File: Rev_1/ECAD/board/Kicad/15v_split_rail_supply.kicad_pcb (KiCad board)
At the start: 4 copper layers, 71.1 x 36.8 mm, 89 parts, among them Q1 NPN, Q100 IPP029N15NM6, Q101 NPN, Q102 NPN, Q103 PMOS, Q2 NPN, U100 LM3478MA, U2 LM358, U3 LM358, U4 SN74AHC1G02DBVR, U5 SN74AHC1G02DBVR

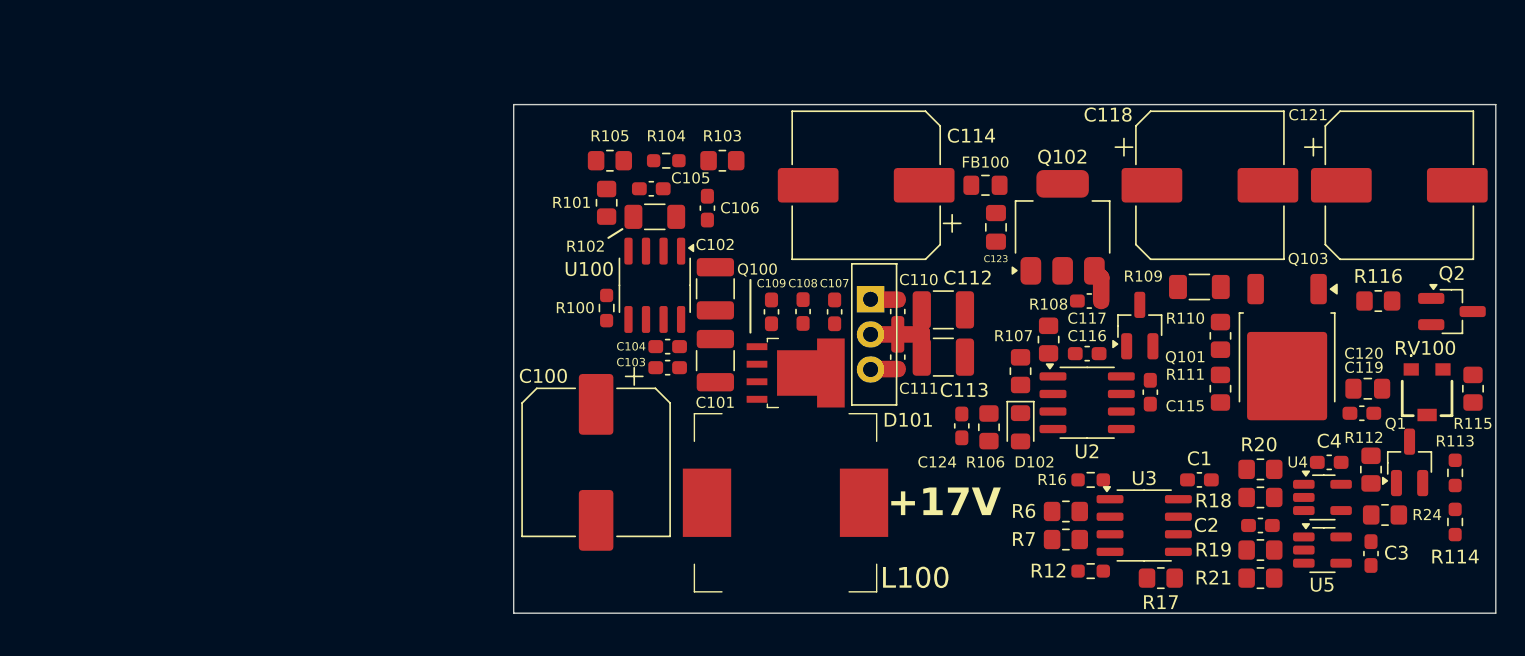
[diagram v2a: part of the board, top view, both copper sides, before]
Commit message: Moved Input Capacitors to minimize loop area and created pours for boost converter
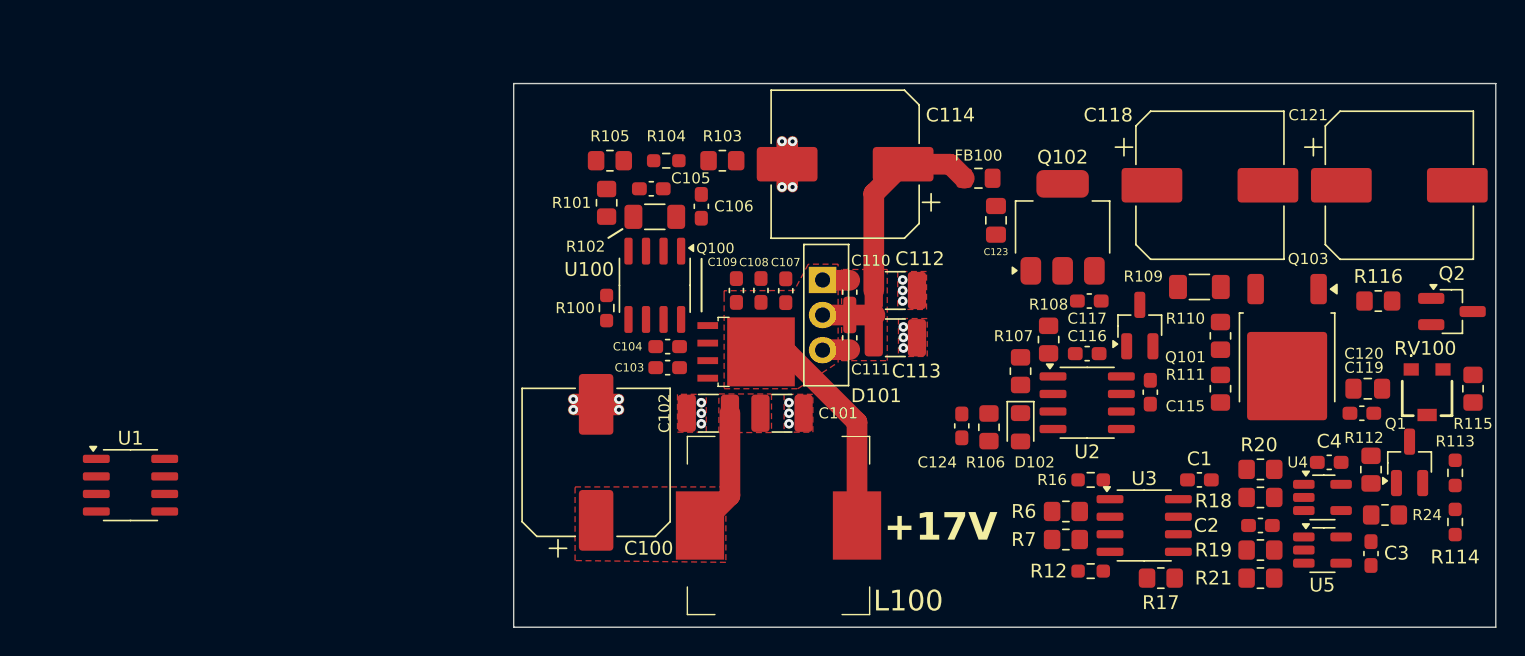
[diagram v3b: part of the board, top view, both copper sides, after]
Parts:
- added U1: LM3478MA, Package_SO:SOIC-8_3.9x4.9mm_P1.27mm, F.Cu at (85.9, 96.9)
- Q100: footprint filip:TO-263-5_TabPin1-HandSoldered -> filip:TO-263-4_TabPin1-HandSoldered
- moved C102 9.03 mm to (127.8, 91.7), turned to 180 degrees
- moved C101 6.15 mm to (133.1, 91.7), turned to 0 degrees
- moved C107 3.85 mm to (133.4, 82.8)
- moved C110 3.75 mm to (138.0, 82.9)
- moved C111 3.75 mm to (138.0, 86.2)
- moved C112 3.75 mm to (141.3, 82.8)
- moved C113 3.75 mm to (141.3, 86.2)
- moved D101 3.75 mm to (136.0, 82.0)
- moved Q100 3.72 mm to (130.4, 87.2)
- moved C108 3.41 mm to (131.6, 82.8)
- moved C109 2.97 mm to (129.8, 82.8)
- moved C114 2.16 mm to (137.7, 73.7)
- moved L100 1.72 mm to (132.8, 99.8)
- moved FB100 0.72 mm to (147.3, 74.7)
- moved C123 0.51 mm to (148.6, 77.7)
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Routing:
- net /+15V DC-DC Converter/SW: track 3.95 -> 21.5 mm
- net GND: track 0.00 -> 14.5 mm, vias 0 -> 20
- net /+15V DC-DC Converter/LOOP_OUT: track 5.78 -> 18.7 mm
- net /+15V DC-DC Converter/V_IN: track 0.00 -> 9.55 mm
- net /+15V DC-DC Converter/SHUNT_IN: track 2.39 -> 0.00 mm
- added copper zone on F.Cu, net /+15V DC-DC Converter/LOOP_OUT
- added copper zone on F.Cu, net /+15V DC-DC Converter/SW
- added copper zone on F.Cu, net /+15V DC-DC Converter/V_IN
- added copper zone on F.Cu, net GND
- added copper zone on In1.Cu, net GND
- added copper zone on In2.Cu, net GND
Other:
- board size 71.1 x 36.8 mm -> 71.1 x 39.4 mm

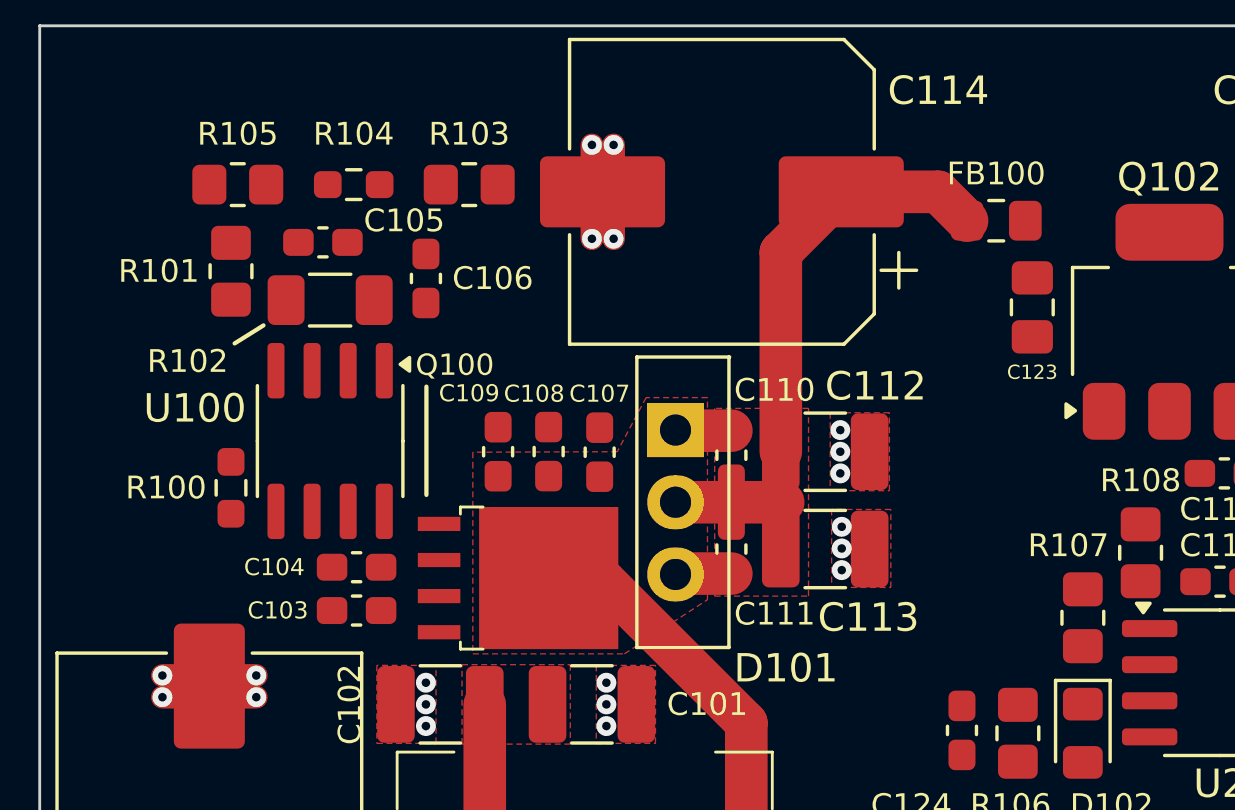
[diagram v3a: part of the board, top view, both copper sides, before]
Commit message: Routed DC-DC Converter, needs to be looked at
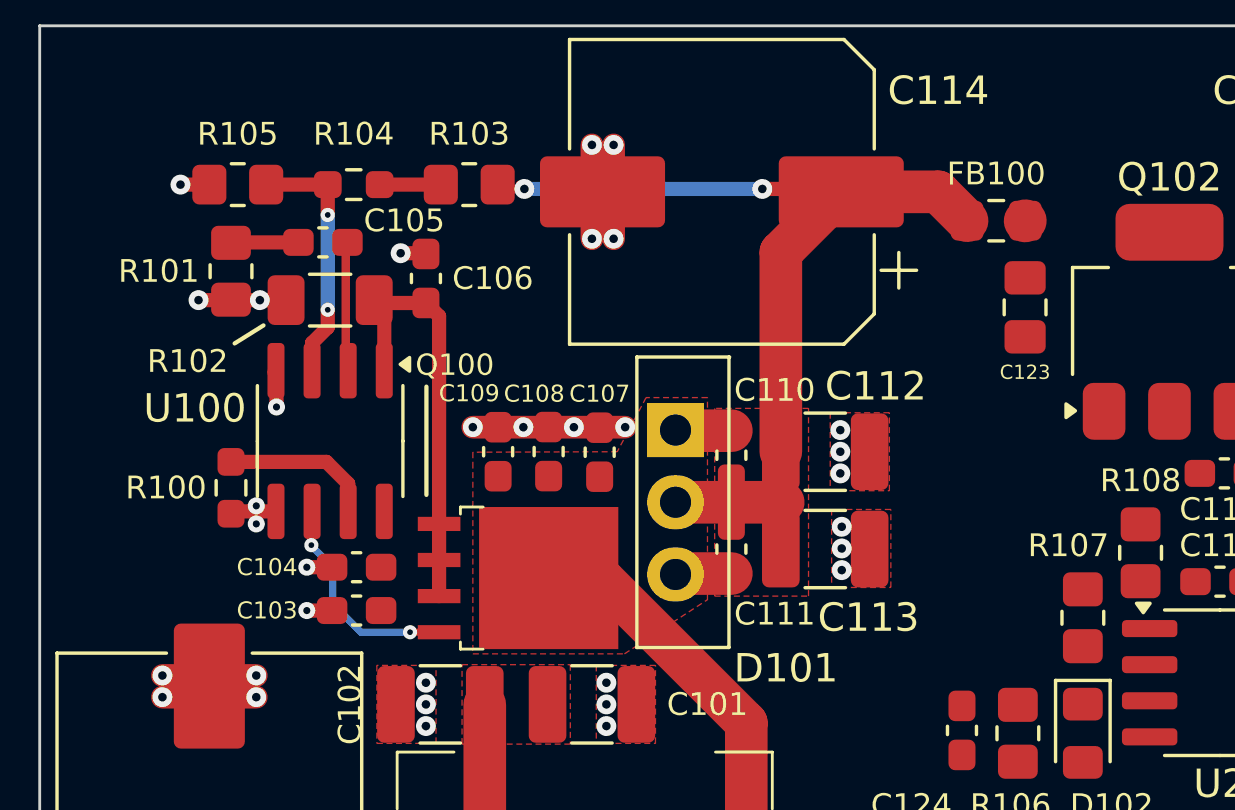
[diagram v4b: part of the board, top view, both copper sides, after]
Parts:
- moved C123 0.25 mm to (148.3, 77.7)
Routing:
- net GND: track 14.5 -> 30.5 mm, vias 20 -> 33
- net /+15V DC-DC Converter/ISEN: track 0.00 -> 15.0 mm
- net /+15V DC-DC Converter/LOOP_OUT: track 18.7 -> 31.1 mm, vias 0 -> 2
- net /+15V DC-DC Converter/FB: track 0.00 -> 9.11 mm, vias 0 -> 2
- net /+15V DC-DC Converter/DR: track 0.00 -> 7.73 mm, vias 0 -> 2
- net /+15V DC-DC Converter/FA/SD: track 0.00 -> 5.42 mm
- net /+15V DC-DC Converter/COMP: track 0.00 -> 4.58 mm
- net /+15V DC-DC Converter/COMP_R2: track 0.00 -> 2.38 mm
- net /+15V DC-DC Converter/DIV: track 0.00 -> 2.15 mm

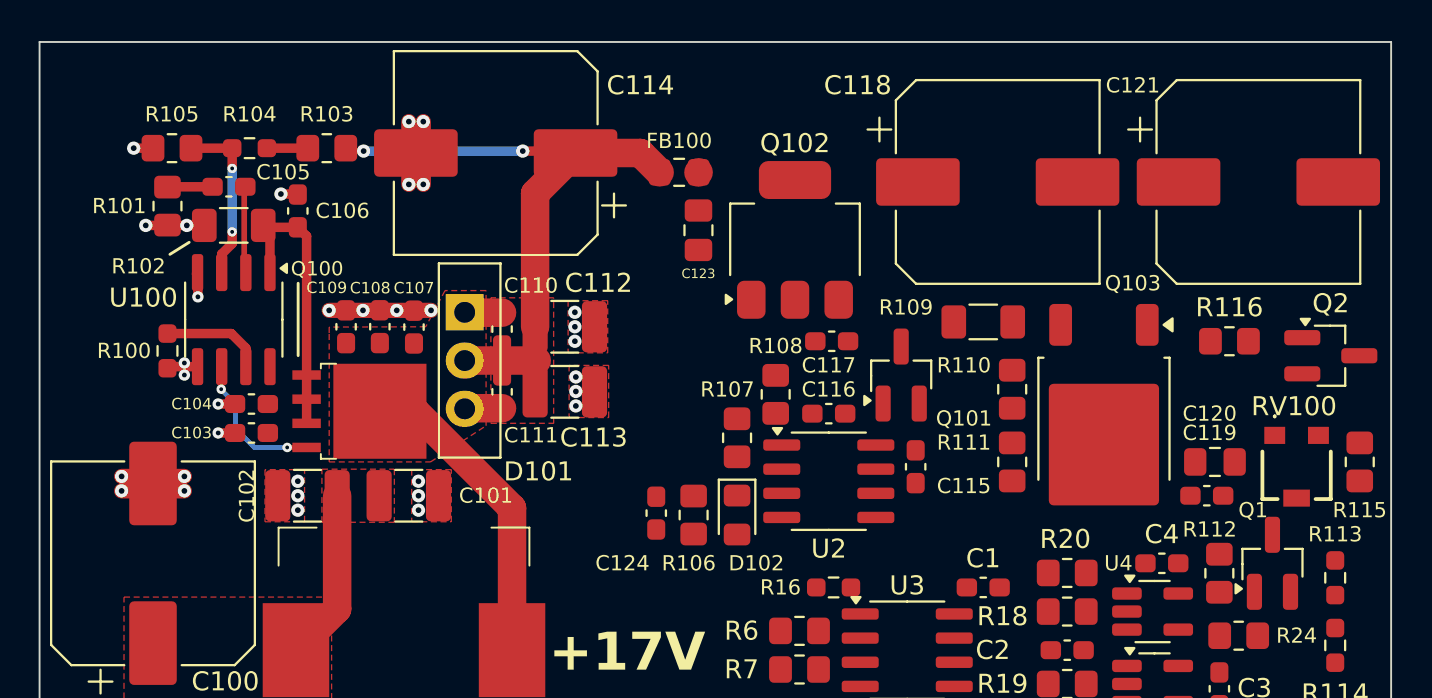
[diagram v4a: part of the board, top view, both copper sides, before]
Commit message: Routed 15V regulator
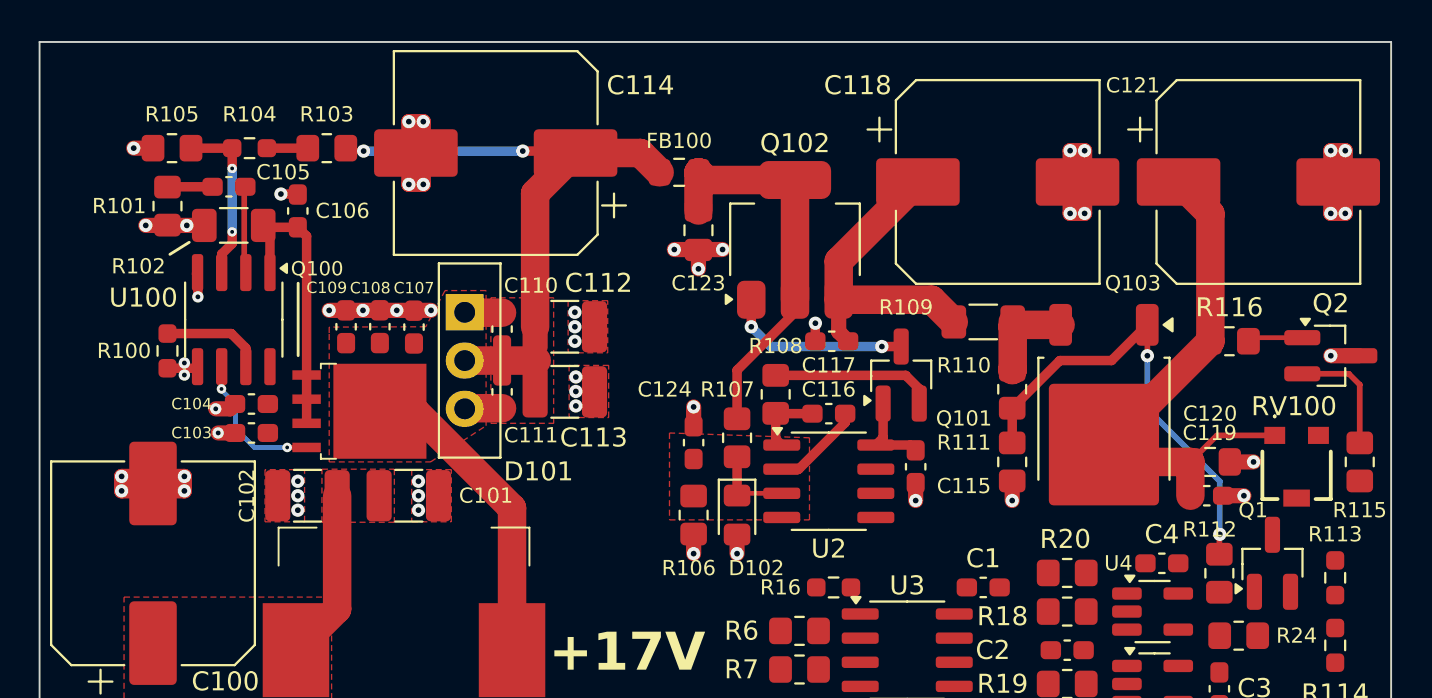
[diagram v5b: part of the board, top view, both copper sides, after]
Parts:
- moved C124 4.20 mm to (148.1, 88.9), turned to 90 degrees
- moved C120 0.25 mm to (175.3, 89.9)
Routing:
- net GND: track 30.5 -> 60.5 mm, vias 33 -> 53
- net +15V: track 0.00 -> 28.7 mm
- net +17V: track 0.01 -> 25.6 mm
- net /+15V DC-DC Converter/MOS_G: track 0.00 -> 24.4 mm, vias 0 -> 2
- net /+15V DC-DC Converter/SHUNT_IN: track 0.00 -> 16.9 mm
- net Net-(Q101-E): track 0.00 -> 9.74 mm, vias 0 -> 2
- net Net-(Q101-B): track 0.00 -> 8.62 mm
- net Net-(Q2-B): track 0.00 -> 6.33 mm
- net /+15V DC-DC Converter/SHUNT_OUT: track 0.00 -> 5.11 mm
- net /+15V DC-DC Converter/V_FB: track 0.00 -> 4.83 mm
- net /+15V DC-DC Converter/V_REF: track 0.00 -> 4.44 mm
- net Net-(C116-Pad1): track 0.00 -> 3.74 mm
- net Net-(Q2-C): track 0.00 -> 2.91 mm
- added copper zone on F.Cu, net /+15V DC-DC Converter/V_REF

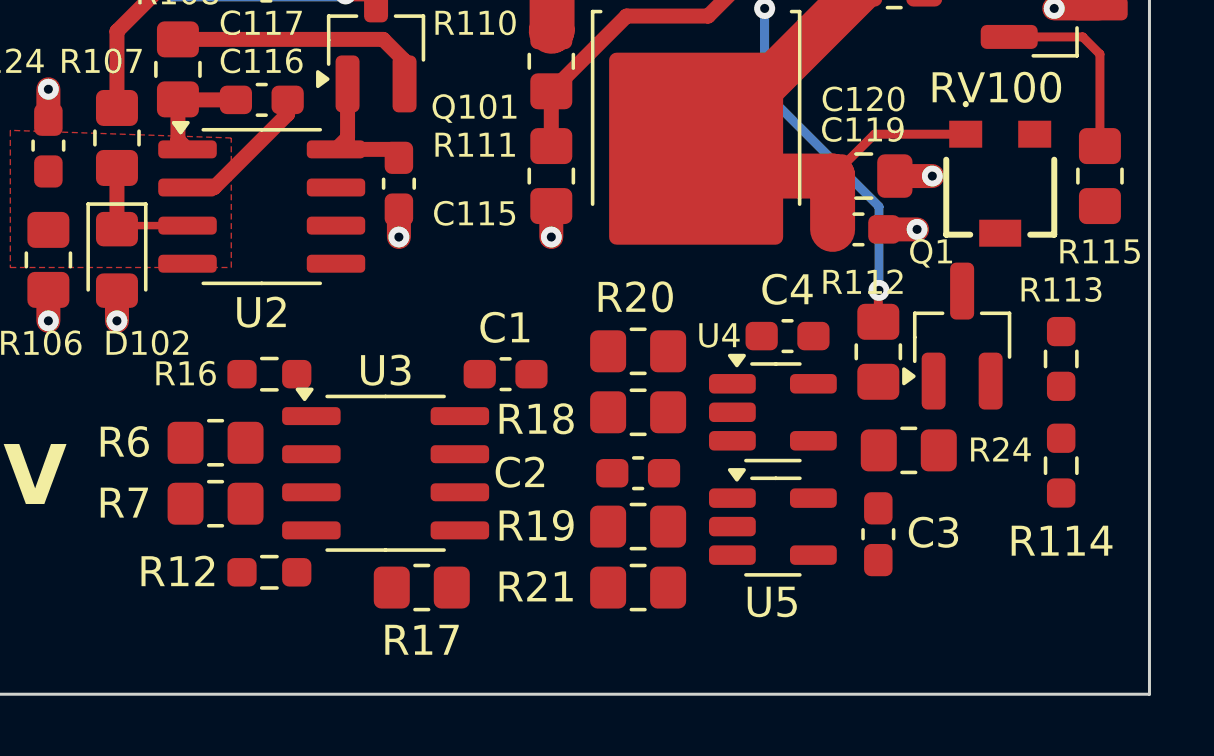
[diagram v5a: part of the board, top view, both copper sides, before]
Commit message: Routed overcurrent logic
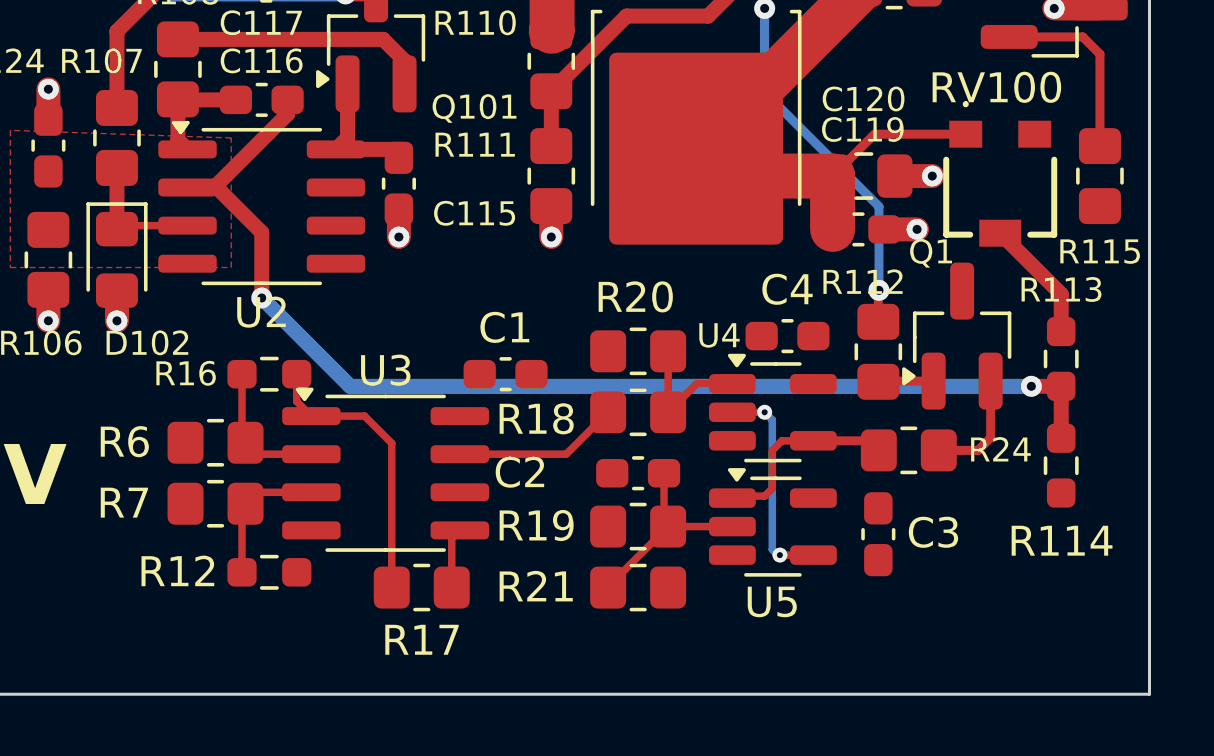
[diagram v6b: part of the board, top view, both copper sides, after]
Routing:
- net /+15V DC-DC Converter/V_FB: track 4.83 -> 39.7 mm, vias 0 -> 2
- net /+15V DC-DC Converter/DIFF_OUT: track 0.00 -> 9.46 mm
- net /+15V DC-DC Converter/#Q: track 0.00 -> 7.20 mm, vias 0 -> 2
- net /+15V DC-DC Converter/RESET: track 0.00 -> 6.84 mm
- net /+15V DC-DC Converter/Q: track 0.00 -> 6.55 mm
- net /+15V DC-DC Converter/SET_SIG: track 0.00 -> 5.52 mm
- net /+15V DC-DC Converter/DIFF_NEG: track 0.00 -> 4.69 mm
- net /+15V DC-DC Converter/DIFF_POS: track 0.00 -> 4.69 mm
- net /+15V DC-DC Converter/SET: track 0.00 -> 4.57 mm
- net Net-(R113-Pad1): track 0.00 -> 4.12 mm
- net /+15V DC-DC Converter/NPN_B: track 0.00 -> 3.79 mm
- net /+15V DC-DC Converter/V_DIFF: track 0.00 -> 2.02 mm
- net /+15V DC-DC Converter/SHUTDOWN: track 0.00 -> 1.85 mm
